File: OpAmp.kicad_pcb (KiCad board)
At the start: 2 copper layers, 53 x 35 mm, 46 parts, among them J1 Conn_01x07, J2 Conn_01x02, J3 Conn_01x02, Q1 5551, Q10 5401, Q11 5551, Q12 TIP42, Q13 5551, Q14 5401, Q15 5551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

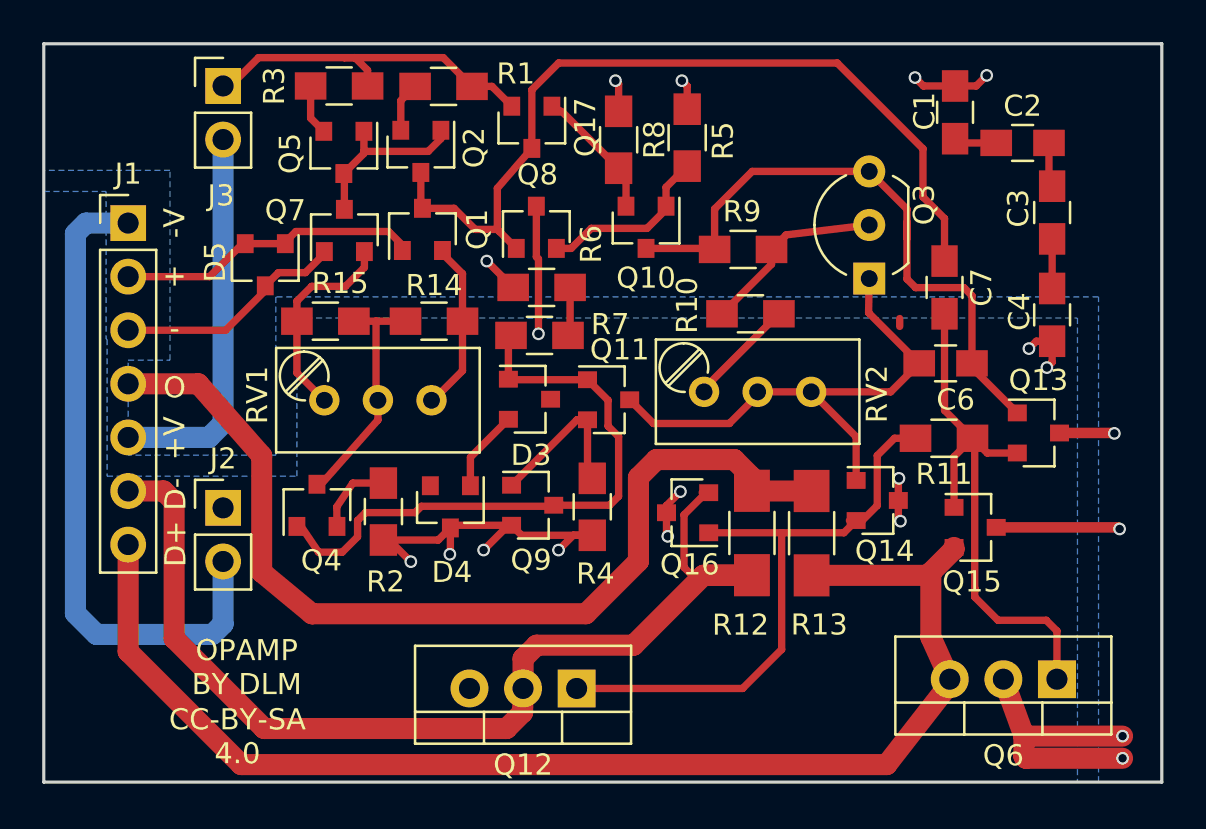
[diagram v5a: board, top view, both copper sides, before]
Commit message: Fixed pinout on TIP42
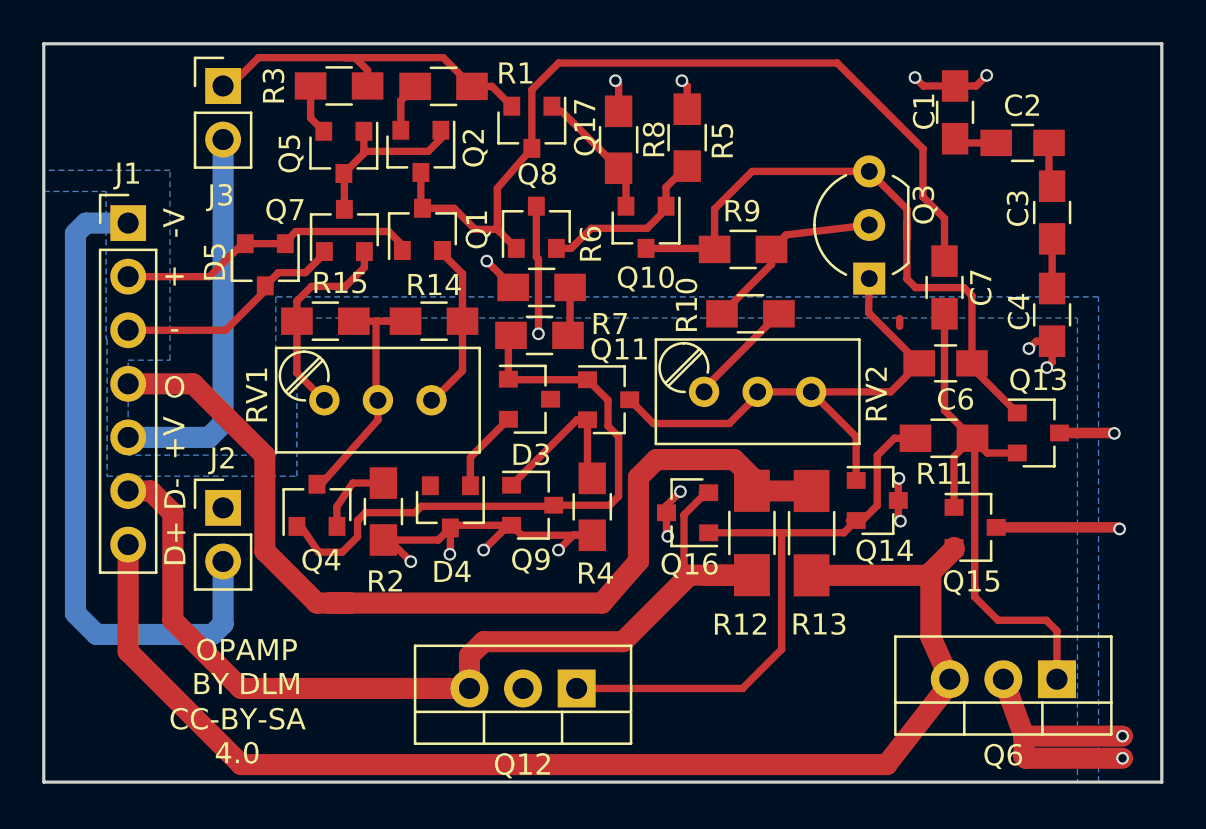
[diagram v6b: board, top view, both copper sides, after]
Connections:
- Q12 pad 2: /DRVMINUS -> VEE
- Q12 pad 3: VEE -> /DRVMINUS
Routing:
- net /DRVMINUS: track 50.5 -> 47.6 mm
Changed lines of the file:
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@@
     (thickness 1.6)
     (drawings 13)
-    (tracks 333)
+    (tracks 332)
     (zones 0)
     (modules 46)
@@
   )
   (setup
-    (last_trace_width 0.35)
+    (last_trace_width 1)
     (user_trace_width 0.35)
     (user_trace_width 0.5)
@@
       (net 25 "Net-(Q12-Pad1)"))
     (pad 2 thru_hole oval (at 2.54 0 180) (size 1.8 1.8) (drill 1) (layers *.Cu *.Mask)
+      (net 5 VEE))
+    (pad 3 thru_hole oval (at 5.08 0 180) (size 1.8 1.8) (drill 1) (layers *.Cu *.Mask)
       (net 28 /DRVMINUS))
-    (pad 3 thru_hole oval (at 5.08 0 180) (size 1.8 1.8) (drill 1) (layers *.Cu *.Mask)
-      (net 5 VEE))
     (model ${KISYS3DMOD}/TO_SOT_Packages_THT.3dshapes/TO-220-3_Vertical.wrl
       (at (xyz 0.1 0 0))
@@
   (segment (start 53.28 70.3) (end 53 70.58) (width 0.35) (layer F.Cu) (net 13))
   (segment (start 53 70.58) (end 53 70.7) (width 0.35) (layer F.Cu) (net 13) (status 30))
-  (segment (start 61.75 84.02) (end 61.71 84.02) (width 1) (layer F.Cu) (net 14))
-  (segment (start 56.33 73.12) (end 53 73.12) (width 1) (layer F.Cu) (net 14))
-  (segment (start 59.33 76.53) (end 56.33 73.12) (width 1) (layer F.Cu) (net 14))
-  (segment (start 59.33 82.05) (end 59.33 76.53) (width 1) (layer F.Cu) (net 14))
-  (segment (start 61.71 84.02) (end 59.33 82.05) (width 1) (layer F.Cu) (net 14))
-  (segment (start 82.57 78.19) (end 82.57 77.55) (width 1) (layer F.Cu) (net 14))
+  (segment (start 63.54 83.512) (end 61.942 83.512) (width 1) (layer F.Cu) (net 14))
+  (segment (start 56.08 73.12) (end 53 73.12) (width 1) (layer F.Cu) (net 14))
+  (segment (start 59.48 76.52) (end 56.08 73.12) (width 1) (layer F.Cu) (net 14))
+  (segment (start 59.48 81.05) (end 59.48 76.52) (width 1) (layer F.Cu) (net 14))
+  (segment (start 61.942 83.512) (end 59.48 81.05) (width 1) (layer F.Cu) (net 14))
+  (segment (start 75.462 83.512) (end 63.54 83.512) (width 1) (layer F.Cu) (net 14))
+  (segment (start 63.54 83.512) (end 62.512 83.512) (width 1) (layer F.Cu) (net 14))
+  (segment (start 77.19 81.53) (end 75.462 83.512) (width 1) (layer F.Cu) (net 14))
+  (segment (start 81.73 76.71) (end 78.04 76.71) (width 1) (layer F.Cu) (net 14))
   (segment (start 82.57 77.55) (end 81.73 76.71) (width 1) (layer F.Cu) (net 14))
-  (segment (start 74.7 84.02) (end 61.75 84.02) (width 1) (layer F.Cu) (net 14))
-  (segment (start 77.19 81.53) (end 74.7 84.02) (width 1) (layer F.Cu) (net 14))
   (segment (start 77.19 77.56) (end 77.19 81.53) (width 1) (layer F.Cu) (net 14))
   (segment (start 78.04 76.71) (end 77.19 77.56) (width 1) (layer F.Cu) (net 14))
-  (segment (start 81.73 76.71) (end 78.04 76.71) (width 1) (layer F.Cu) (net 14))
+  (segment (start 82.57 78.19) (end 82.57 77.55) (width 1) (layer F.Cu) (net 14))
   (segment (start 85.4 78.2) (end 82.58 78.2) (width 1) (layer F.Cu) (net 14))
   (segment (start 82.58 78.2) (end 82.57 78.19) (width 1) (layer F.Cu) (net 14))
@@
   (segment (start 80.3 73.5) (end 80.3 73.35) (width 0.35) (layer F.Cu) (net 27))
   (segment (start 80.3 73.5) (end 80.3 73.4) (width 0.35) (layer F.Cu) (net 27) (status 30))
-  (segment (start 82.57 82.19) (end 80.28 82.19) (width 1) (layer F.Cu) (net 28))
-  (segment (start 71.72 86.15) (end 71.72 87.56) (width 1) (layer F.Cu) (net 28))
-  (segment (start 72.36 85.51) (end 71.72 86.15) (width 1) (layer F.Cu) (net 28))
-  (segment (start 76.96 85.51) (end 72.36 85.51) (width 1) (layer F.Cu) (net 28))
-  (segment (start 80.28 82.19) (end 76.96 85.51) (width 1) (layer F.Cu) (net 28))
+  (segment (start 69.18 86.014) (end 69.18 87.56) (width 1) (layer F.Cu) (net 28))
+  (segment (start 82.57 82.19) (end 79.608 82.19) (width 1) (layer F.Cu) (net 28))
+  (segment (start 79.608 82.19) (end 76.454 85.344) (width 1) (layer F.Cu) (net 28))
+  (segment (start 76.454 85.344) (end 69.85 85.344) (width 1) (layer F.Cu) (net 28))
+  (segment (start 69.85 85.344) (end 69.18 86.014) (width 1) (layer F.Cu) (net 28))
+  (segment (start 53 78.2) (end 54.07 78.2) (width 1) (layer F.Cu) (net 28))
+  (segment (start 54.07 78.2) (end 55.118 79.248) (width 1) (layer F.Cu) (net 28))
+  (segment (start 55.118 79.248) (end 55.118 84.328) (width 1) (layer F.Cu) (net 28))
+  (segment (start 55.118 84.328) (end 58.35 87.56) (width 1) (layer F.Cu) (net 28))
+  (segment (start 58.35 87.56) (end 69.18 87.56) (width 1) (layer F.Cu) (net 28))
   (segment (start 80.38 82.19) (end 79.72 82.19) (width 0.35) (layer F.Cu) (net 28))
   (segment (start 79.35 79.33) (end 80.4 78.28) (width 0.35) (layer F.Cu) (net 28))
@@
   (segment (start 79.72 82.19) (end 79.35 81.82) (width 0.35) (layer F.Cu) (net 28))
   (segment (start 82.57 82.19) (end 80.38 82.19) (width 1) (layer F.Cu) (net 28))
-  (segment (start 71.72 87.56) (end 71.7 88.7) (width 1) (layer F.Cu) (net 28) (status 10))
-  (segment (start 71.7 88.7) (end 70.94 89.46) (width 1) (layer F.Cu) (net 28))
-  (segment (start 70.94 89.46) (end 59.45 89.46) (width 1) (layer F.Cu) (net 28))
-  (segment (start 59.45 89.46) (end 55.18 85.19) (width 1) (layer F.Cu) (net 28))
-  (segment (start 55.18 85.19) (end 55.18 78.7) (width 1) (layer F.Cu) (net 28))
-  (segment (start 55.18 78.7) (end 54.68 78.2) (width 1) (layer F.Cu) (net 28))
-  (segment (start 54.68 78.2) (end 53 78.2) (width 1) (layer F.Cu) (net 28))
   (segment (start 80.4 78.28) (end 80.52 78.28) (width 0.35) (layer F.Cu) (net 28))
   (segment (start 80.21 78.28) (end 80.52 78.28) (width 0.35) (layer F.Cu) (net 28))
